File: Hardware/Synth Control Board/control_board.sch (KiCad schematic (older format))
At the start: 34 parts, among them SW10 SW_SPST, SW11 SW_SPST, SW12 SW_SPST, SW13 SW_SPST, SW2 SW_SPST, SW3 SW_SPST, SW4 SW_SPST, SW5 SW_SPST, SW6 SW_SPST, SW7 SW_SPST, SW8 SW_SPST, SW9 SW_SPST

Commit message: connect control board to main synth schem pages
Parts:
- removed J? (x4): Conn_01x12, symbol Conn_01x12
- added J? (x4): Conn_01x13, symbol Conn_01x13
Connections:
- net labels added: freq_fb_1, freq_fb_2, freq_fb_3, freq_fb_4
- wire segments 116 -> 125
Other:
- moved on the sheet: J?, SW2, SW3, SW4, SW5, SW6, SW7, SW8, SW9

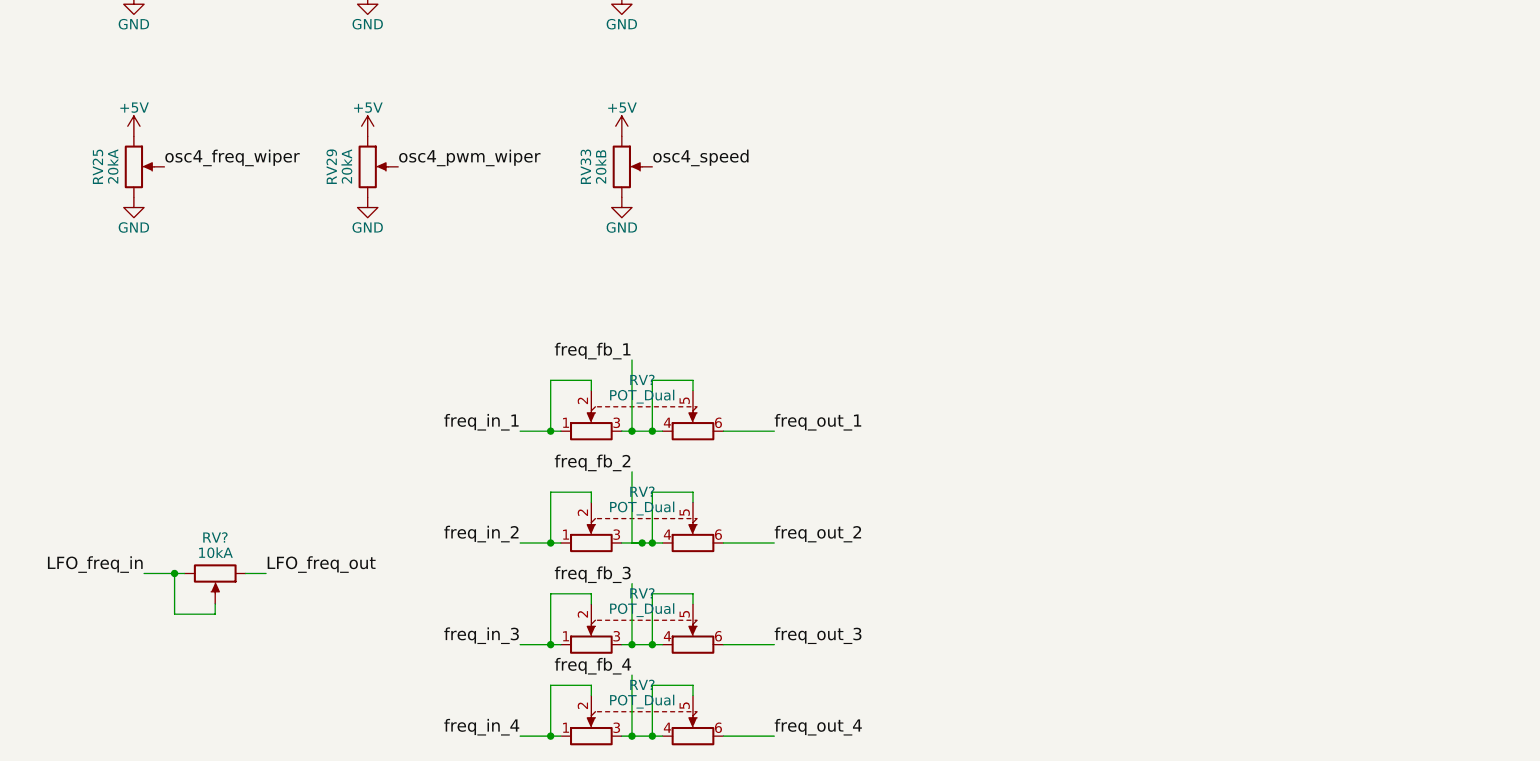
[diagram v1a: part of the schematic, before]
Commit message: add connectors for capsense buttons and LFO shape switch
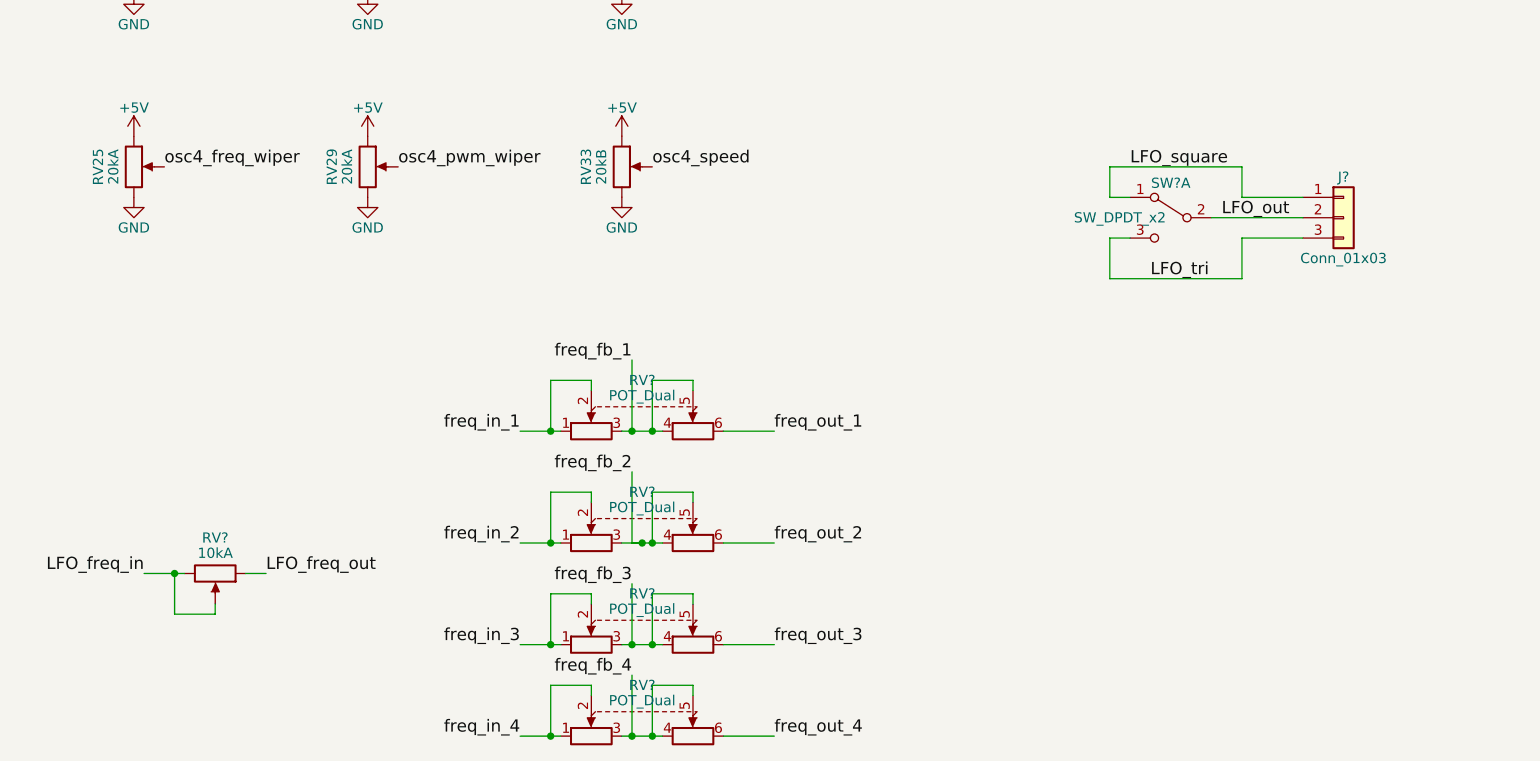
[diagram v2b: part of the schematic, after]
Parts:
- added J?: Conn_01x03, symbol Conn_01x03
- added SW?: SW_DPDT_x2, symbol SW_DPDT_x2
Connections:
- new net LFO_out: J?.2 (Pin_2), SW?.2 (B)
- new net LFO_square: J?.1 (Pin_1), SW?.1 (A)
- new net LFO_tri: J?.3 (Pin_3), SW?.3 (C)
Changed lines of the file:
@@
 	3150 5400 3150 5650
 Wire Wire Line
-	3000 5650 3200 5650
+	3000 5650 3150 5650
+Wire Wire Line
+	3150 5650 3200 5650
 Connection ~ 3150 5650
 Wire Wire Line
@@
 	3650 5400 3650 5650
 Wire Wire Line
-	3500 5650 3700 5650
+	3500 5650 3550 5650
+Wire Wire Line
+	3550 5650 3650 5650
+Wire Wire Line
+	3650 5650 3700 5650
 Connection ~ 3650 5650
 Wire Wire Line
@@
 	3150 5950 3150 6200
 Wire Wire Line
-	3000 6200 3200 6200
+	3000 6200 3150 6200
+Wire Wire Line
+	3150 6200 3200 6200
 Connection ~ 3150 6200
 Wire Wire Line
-	3500 6200 3700 6200
+	3500 6200 3600 6200
+Wire Wire Line
+	3600 6200 3650 6200
+Wire Wire Line
+	3650 6200 3700 6200
 Wire Wire Line
 	3850 6000 3850 5950
@@
 	3150 6450 3150 6700
 Wire Wire Line
-	3000 6700 3200 6700
+	3000 6700 3150 6700
+Wire Wire Line
+	3150 6700 3200 6700
 Connection ~ 3150 6700
 Wire Wire Line
-	3500 6700 3700 6700
+	3500 6700 3550 6700
+Wire Wire Line
+	3550 6700 3650 6700
+Wire Wire Line
+	3650 6700 3700 6700
 Wire Wire Line
 	3850 6500 3850 6450
@@
 	4000 6700 4250 6700
 Wire Wire Line
-	3500 7150 3700 7150
-Wire Wire Line
-	3000 7150 3200 7150
+	3500 7150 3550 7150
+Wire Wire Line
+	3550 7150 3650 7150
+Wire Wire Line
+	3650 7150 3700 7150
+Wire Wire Line
+	3000 7150 3150 7150
+Wire Wire Line
+	3150 7150 3200 7150
 Wire Wire Line
 	4000 7150 4250 7150
@@
 	1300 6550 1300 6350
 Wire Wire Line
-	1150 6350 1350 6350
+	1150 6350 1300 6350
+Wire Wire Line
+	1300 6350 1350 6350
 Connection ~ 1300 6350
 Wire Wire Line
@@
 Wire Wire Line
 	10900 2600 10700 2600
+$Comp
+L SW_DPDT_x2 SW?
+U 1 1 5C5E11B0
+P 6200 4600
+F 0 "SW?" H 6200 4770 50  0000 C CNN
+F 1 "SW_DPDT_x2" H 6450 4600 50  0000 C CNN
+F 2 "" H 6200 4600 50  0001 C CNN
+F 3 "" H 6200 4600 50  0001 C CNN
+	1    6200 4600
+	-1   0    0    -1
+$EndComp
+$Comp
+L Conn_01x03 J?
+U 1 1 5C5E130C
+P 7050 4600
+F 0 "J?" H 7050 4800 50  0000 C CNN
+F 1 "Conn_01x03" H 7050 4400 50  0000 C CNN
+F 2 "" H 7050 4600 50  0001 C CNN
+F 3 "" H 7050 4600 50  0001 C CNN
+	1    7050 4600
+	1    0    0    -1
+$EndComp
+Wire Wire Line
+	6850 4600 6400 4600
+Wire Wire Line
+	6850 4500 6550 4500
+Wire Wire Line
+	6550 4500 6550 4350
+Wire Wire Line
+	6550 4350 5900 4350
+Wire Wire Line
+	5900 4350 5900 4500
+Wire Wire Line
+	5900 4500 6000 4500
+Wire Wire Line
+	6000 4700 5900 4700
+Wire Wire Line
+	5900 4700 5900 4900
+Wire Wire Line
+	5900 4900 6550 4900
+Wire Wire Line
+	6550 4900 6550 4700
+Wire Wire Line
+	6550 4700 6850 4700
+Text Label 6000 4350 0    60   ~ 0
+LFO_square
+Text Label 6100 4900 0    60   ~ 0
+LFO_tri
+Text Label 6450 4600 0    60   ~ 0
+LFO_out
 $EndSCHEMATC

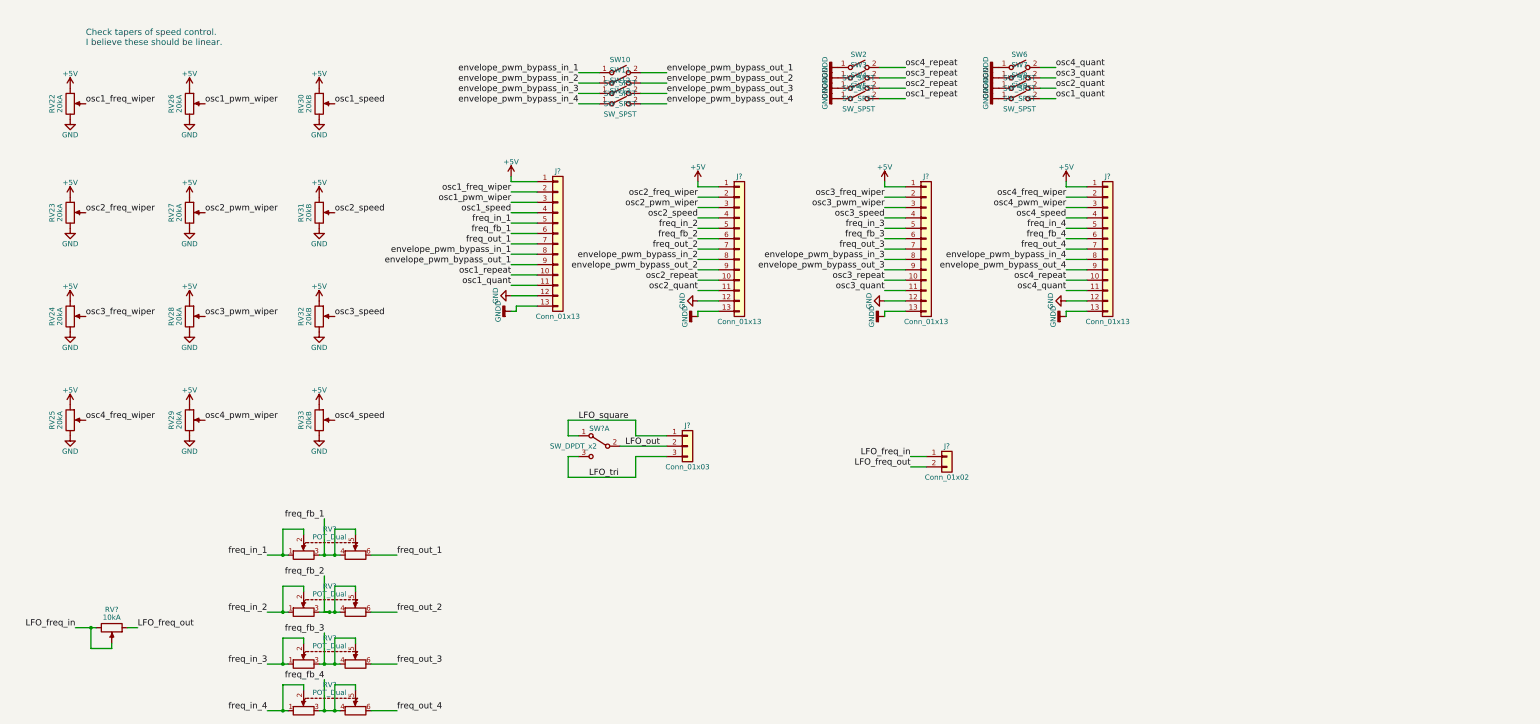
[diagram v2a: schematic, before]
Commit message: add volume pots to control board
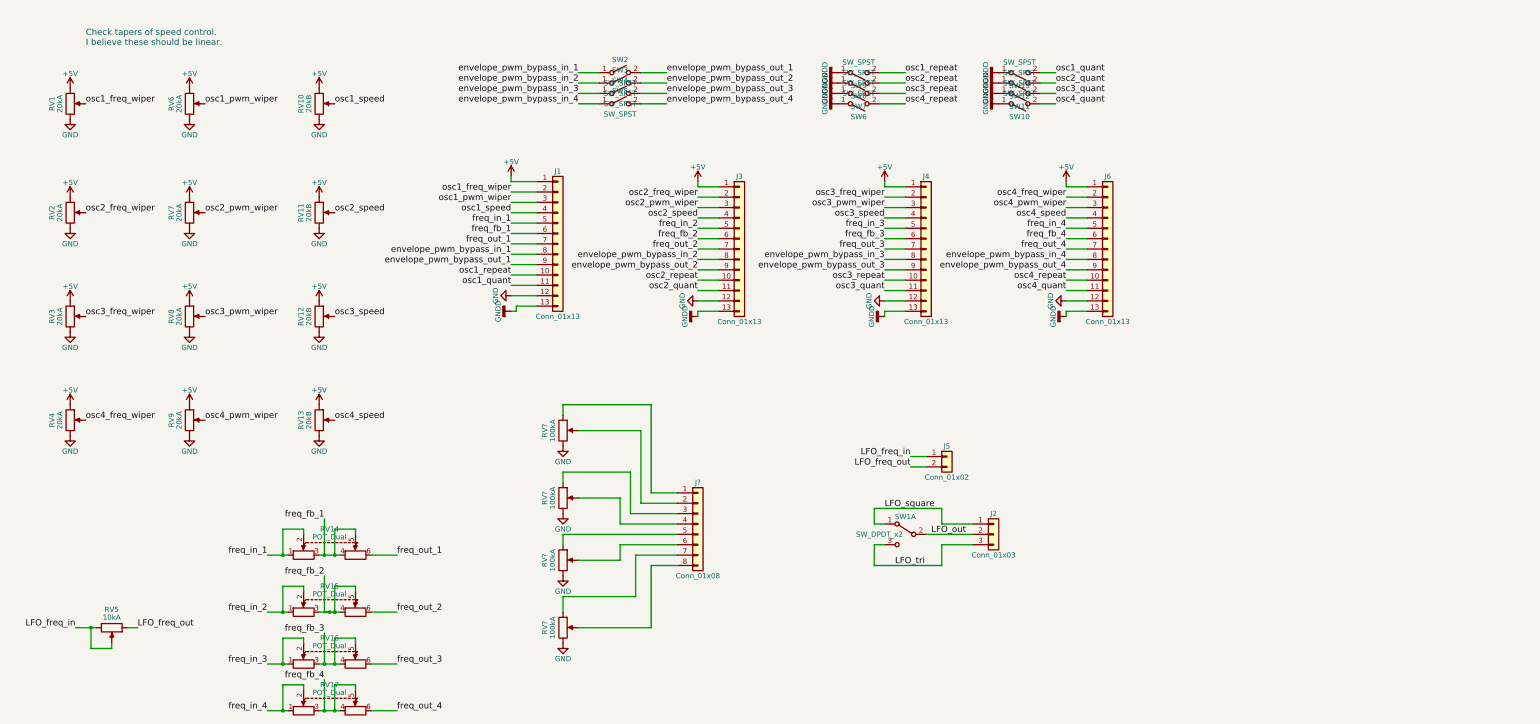
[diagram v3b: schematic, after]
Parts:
- added J?: Conn_01x08, symbol Conn_01x08
- added RV? (x4): 100kA, Potentiometers:Potentiometer_Bourns_PTV09A-1_Horizontal, symbol POT
- J1, J3, J4, J6: renamed from J?; footprint (none) -> Pin_Headers:Pin_Header_Straight_1x13_Pitch2.54mm
- J2: renamed from J?; footprint (none) -> Pin_Headers:Pin_Header_Straight_1x03_Pitch2.54mm
- J5: renamed from J?; footprint (none) -> Pin_Headers:Pin_Header_Straight_1x02_Pitch2.54mm
- RV14, RV15, RV16, RV17: renamed from RV?; footprint (none) -> Potentiometers:Potentiometer_Alps_RK09L_Double_Horizontal
- SW1: renamed from SW?; footprint (none) -> SparkFun-Electromechanical:SWITCH-SPDT
- gave numbers to parts that had none: 1
- renumbered RV22 to RV1, RV30 to RV10, RV31 to RV11, RV32 to RV12, RV33 to RV13, RV23 to RV2, RV24 to RV3, RV25 to RV4, RV26 to RV6, RV27 to RV7, RV28 to RV8, RV29 to RV9, SW6 to SW10, SW7 to SW11, SW8 to SW12, SW9 to SW13, SW10 to SW2, SW11 to SW3, SW12 to SW4, SW13 to SW5, SW2 to SW6, SW3 to SW7, SW4 to SW8, SW5 to SW9
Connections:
- net GND: now also RV?.3, RV?.3, RV?.3, RV?.3
- new net: J?.1 (Pin_1), RV?.1
- new net: J?.2 (Pin_2), RV?.2
- new net: J?.3 (Pin_3), RV?.1
- new net: J?.4 (Pin_4), RV?.2
- new net: J?.5 (Pin_5), RV?.1
- new net: J?.6 (Pin_6), RV?.2
- new net: J?.7 (Pin_7), RV?.1
- new net: J?.8 (Pin_8), RV?.2
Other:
- moved on the sheet: J2, SW10, SW11, SW12, SW13, SW1A, SW6, SW7, SW8, SW9

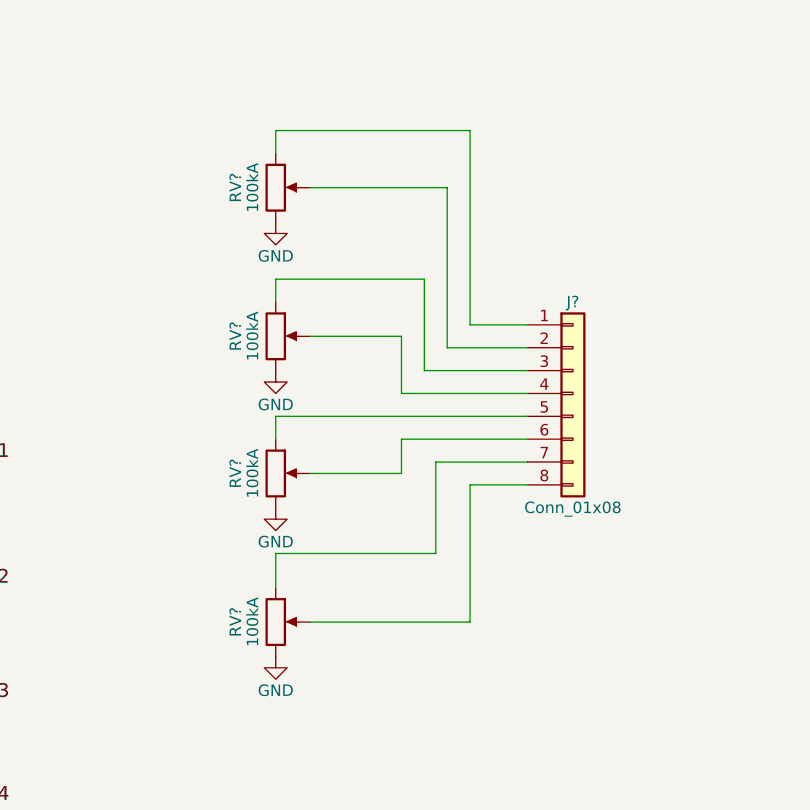
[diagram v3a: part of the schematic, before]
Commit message: place MCU footprints
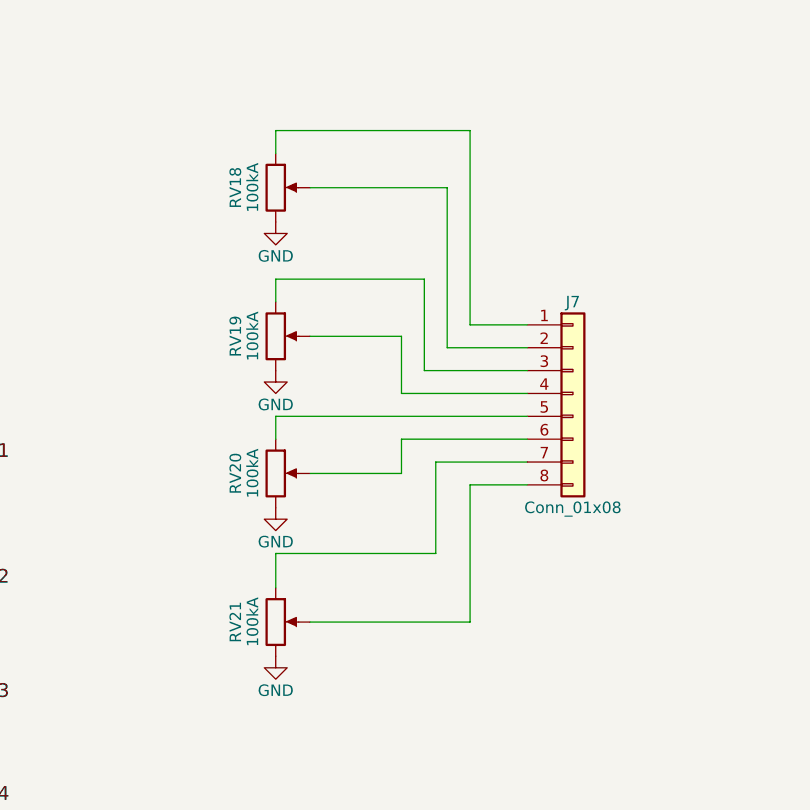
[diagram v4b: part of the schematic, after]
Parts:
- J7: renamed from J?; footprint (none) -> Pin_Headers:Pin_Header_Straight_1x08_Pitch2.54mm
- gave numbers to parts that had none: 4
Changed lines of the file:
@@
 LFO_out
 $Comp
-L POT RV?
+L POT RV18
 U 1 1 5C61E4A8
 P 5850 4450
-F 0 "RV?" V 5675 4450 50  0000 C CNN
+F 0 "RV18" V 5675 4450 50  0000 C CNN
 F 1 "100kA" V 5750 4450 50  0000 C CNN
 F 2 "Potentiometers:Potentiometer_Bourns_PTV09A-1_Horizontal" H 5850 4450 50  0001 C CNN
@@
 $EndComp
 $Comp
-L GND #PWR?
+L GND #PWR045
 U 1 1 5C61E93E
 P 5850 4600
-F 0 "#PWR?" H 5850 4350 50  0001 C CNN
+F 0 "#PWR045" H 5850 4350 50  0001 C CNN
 F 1 "GND" H 5850 4450 50  0000 C CNN
 F 2 "" H 5850 4600 50  0001 C CNN
@@
 $EndComp
 $Comp
-L POT RV?
+L POT RV19
 U 1 1 5C61EA65
 P 5850 5100
-F 0 "RV?" V 5675 5100 50  0000 C CNN
+F 0 "RV19" V 5675 5100 50  0000 C CNN
 F 1 "100kA" V 5750 5100 50  0000 C CNN
 F 2 "Potentiometers:Potentiometer_Bourns_PTV09A-1_Horizontal" H 5850 5100 50  0001 C CNN
@@
 $EndComp
 $Comp
-L GND #PWR?
+L GND #PWR046
 U 1 1 5C61EA6B
 P 5850 5250
-F 0 "#PWR?" H 5850 5000 50  0001 C CNN
+F 0 "#PWR046" H 5850 5000 50  0001 C CNN
 F 1 "GND" H 5850 5100 50  0000 C CNN
 F 2 "" H 5850 5250 50  0001 C CNN
@@
 $EndComp
 $Comp
-L POT RV?
+L POT RV20
 U 1 1 5C61EB63
 P 5850 5700
-F 0 "RV?" V 5675 5700 50  0000 C CNN
+F 0 "RV20" V 5675 5700 50  0000 C CNN
 F 1 "100kA" V 5750 5700 50  0000 C CNN
 F 2 "Potentiometers:Potentiometer_Bourns_PTV09A-1_Horizontal" H 5850 5700 50  0001 C CNN
@@
 $EndComp
 $Comp
-L GND #PWR?
+L GND #PWR047
 U 1 1 5C61EB69
 P 5850 5850
-F 0 "#PWR?" H 5850 5600 50  0001 C CNN
+F 0 "#PWR047" H 5850 5600 50  0001 C CNN
 F 1 "GND" H 5850 5700 50  0000 C CNN
 F 2 "" H 5850 5850 50  0001 C CNN
@@
 $EndComp
 $Comp
-L POT RV?
+L POT RV21
 U 1 1 5C61EB6F
 P 5850 6350
-F 0 "RV?" V 5675 6350 50  0000 C CNN
+F 0 "RV21" V 5675 6350 50  0000 C CNN
 F 1 "100kA" V 5750 6350 50  0000 C CNN
 F 2 "Potentiometers:Potentiometer_Bourns_PTV09A-1_Horizontal" H 5850 6350 50  0001 C CNN
@@
 $EndComp
 $Comp
-L GND #PWR?
+L GND #PWR048
 U 1 1 5C61EB75
 P 5850 6500
-F 0 "#PWR?" H 5850 6250 50  0001 C CNN
+F 0 "#PWR048" H 5850 6250 50  0001 C CNN
 F 1 "GND" H 5850 6350 50  0000 C CNN
 F 2 "" H 5850 6500 50  0001 C CNN
@@
 $EndComp
 $Comp
-L Conn_01x08 J?
+L Conn_01x08 J7
 U 1 1 5C61E895
 P 7150 5350
-F 0 "J?" H 7150 5750 50  0000 C CNN
+F 0 "J7" H 7150 5750 50  0000 C CNN
 F 1 "Conn_01x08" H 7150 4850 50  0000 C CNN
-F 2 "" H 7150 5350 50  0001 C CNN
+F 2 "Pin_Headers:Pin_Header_Straight_1x08_Pitch2.54mm" H 7150 5350 50  0001 C CNN
 F 3 "" H 7150 5350 50  0001 C CNN
 	1    7150 5350
